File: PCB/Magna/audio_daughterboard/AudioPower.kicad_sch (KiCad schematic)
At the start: 40 parts, among them U901 TLV76701DRVx, U902 TLV61046ADBVR, U903 TLV76701DRVx

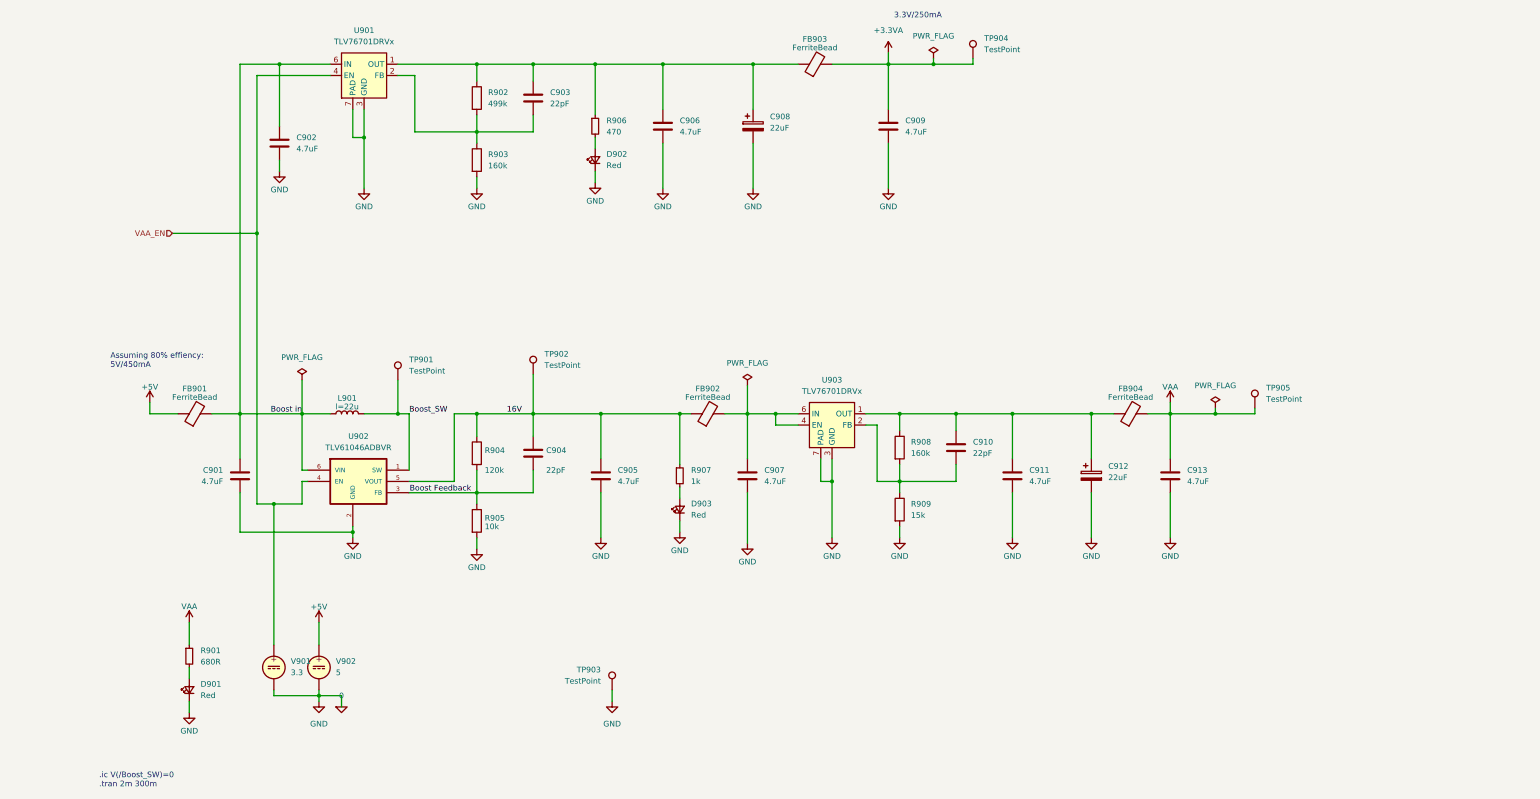
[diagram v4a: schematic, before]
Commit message: Change ADC and add MCU for IO control
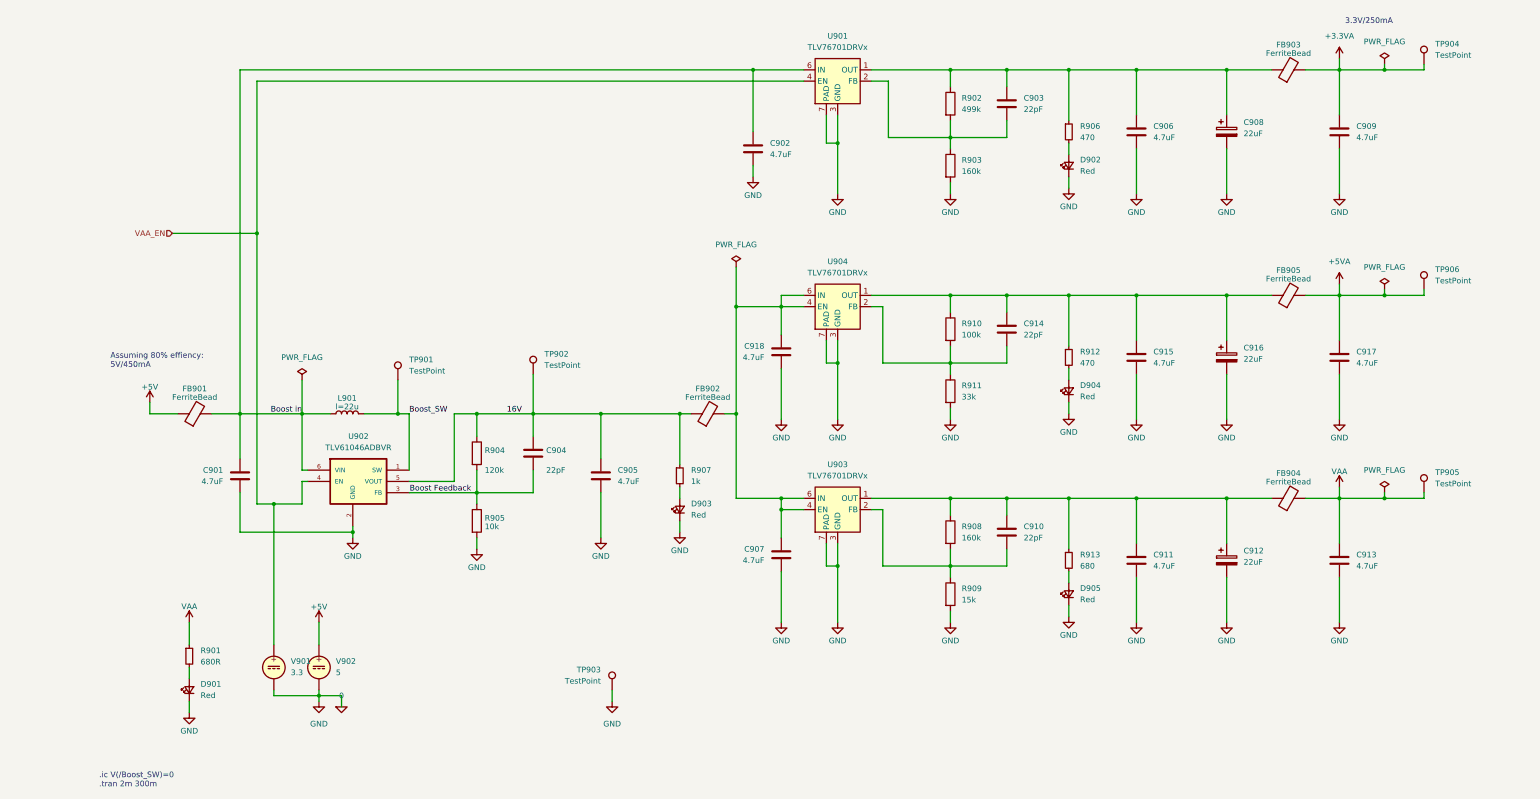
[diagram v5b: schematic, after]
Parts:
- added C914: 22pF, symbol Device:C
- added C915, C917, C918: 4.7uF, Capacitor_SMD:C_0805_2012Metric_Pad1.18x1.45mm_HandSolder, symbol Device:C
- added C916: 22uF, Capacitor_SMD:CP_Elec_5x5.8, symbol Device:C_Polarized
- added D904, D905: Red, Diode_SMD:D_0805_2012Metric_Pad1.15x1.40mm_HandSolder, symbol Device:LED_Small
- added FB905: FerriteBead, Inductor_SMD:L_0805_2012Metric, symbol Device:FerriteBead
- added R910: 100k, symbol Device:R
- added R911: 33k, symbol Device:R
- added R912: 470, Resistor_SMD:R_0805_2012Metric_Pad1.20x1.40mm_HandSolder, symbol Device:R_Small
- added R913: 680, Resistor_SMD:R_0805_2012Metric_Pad1.20x1.40mm_HandSolder, symbol Device:R_Small
- added TP906: TestPoint, TestPoint:TestPoint_Keystone_5005-5009_Compact, symbol Connector:TestPoint
- added U904: TLV76701DRVx, Package_SON:WSON-6-1EP_2x2mm_P0.65mm_EP1x1.6mm_ThermalVias, symbol Regulator_Linear:TLV76701DRVx
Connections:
- net 0: now also C915.2, C916.2, C917.2, C918.2, D904.1 (K), D905.1 (K), R911.2, U904.3 (GND), U904.5 (GND), U904.7 (PAD)
- net at C910.1, C911.1, C912.1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: now also R913.1
- net at C907.1, FB902.2, U903.4 (EN)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: now also C918.1, U904.4 (EN), U904.6 (IN)
- new net: C914.1, C915.1, C916.1, FB905.1, R910.1, R912.1, U904.1 (OUT)
- new net: C914.2, R910.2, R911.1, U904.2 (FB)
- new net: D905.2 (A), R913.2
- new net: D904.2 (A), R912.2
- new net +5VA: C917.1, FB905.2, TP906.1
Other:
- moved on the sheet: C902, C903, C906, C907, C908, C909, C910, C911, C912, C913, D902, FB903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

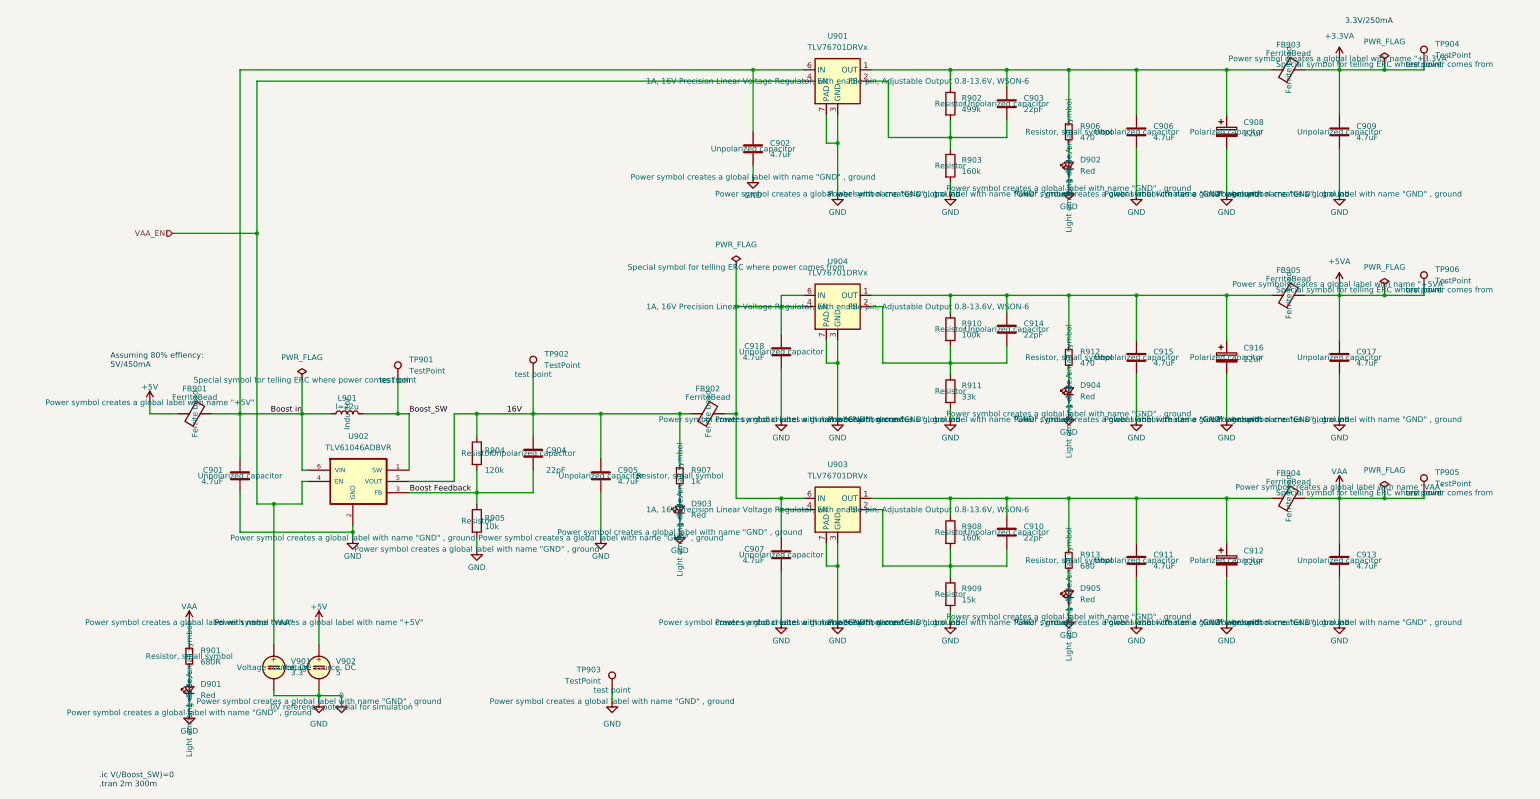
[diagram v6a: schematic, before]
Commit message: Update schematics to Kicad 9
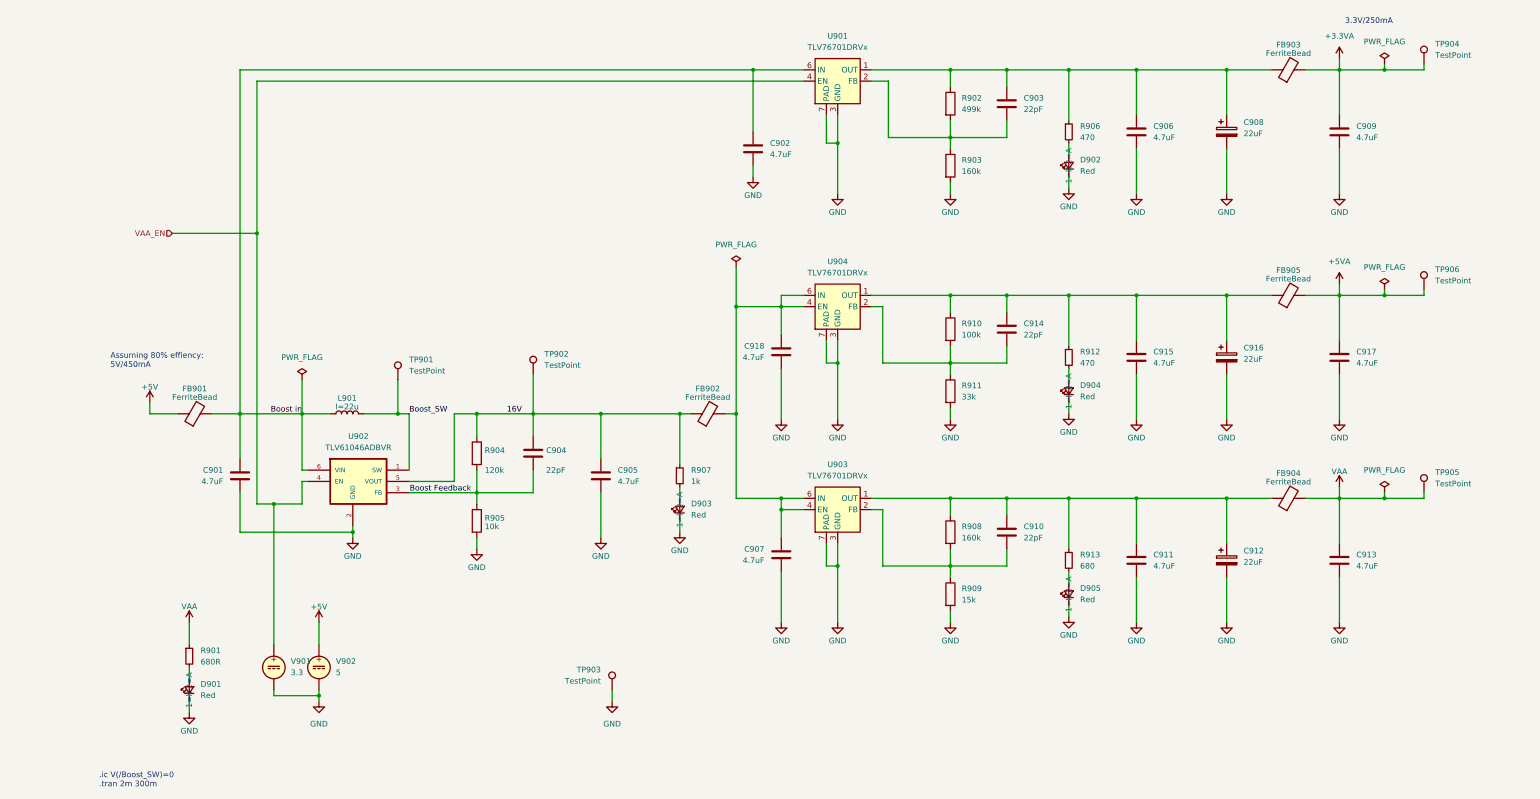
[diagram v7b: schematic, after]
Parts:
- U902: footprint TLV61046ADBVR:SOT95P280X145-6N -> Package_TO_SOT_SMD:TSOT-23-6_HandSoldering
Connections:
- net 0 renamed GND

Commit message: Update audio PCB
Mainly added simulations to Linedriver and DAC.

Also fixed some small issues that was found when simulating
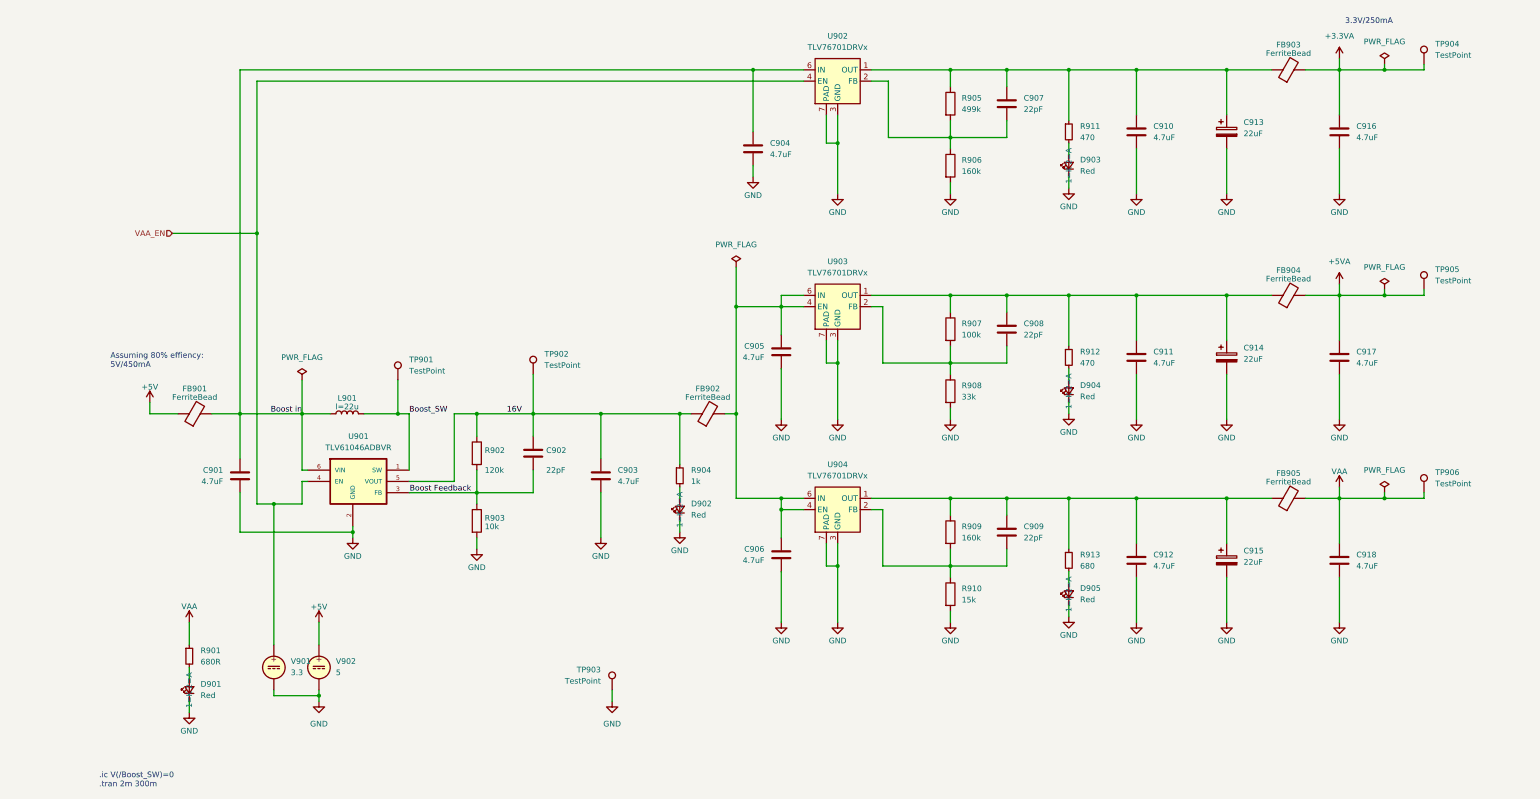
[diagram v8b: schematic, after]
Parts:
- renumbered C904 to C902, C905 to C903, C902 to C904, C918 to C905, C907 to C906, C903 to C907, C914 to C908, C910 to C909, C906 to C910, C915 to C911, C911 to C912, C908 to C913, C916 to C914, C912 to C915, C909 to C916, C913 to C918, D903 to D902, D902 to D903, FB905 to FB904, FB904 to FB905, R904 to R902, R905 to R903, R907 to R904, R902 to R905, R903 to R906, R910 to R907, R911 to R908, R908 to R909, R909 to R910, R906 to R911, TP906 to TP905, TP905 to TP906, U902 to U901, U901 to U902, U904 to U903, U903 to U904
